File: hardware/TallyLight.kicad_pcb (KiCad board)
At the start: 4 copper layers, 68 x 68 mm, 167 parts, among them J1 Hanrun HY931147C, J2 USB_C_Receptacle_USB2.0, J3 Strapping, SW1 SW_Push, T2 HR051067, U10 EL357N(B)(TA)-G, U11 CJ431, U2 KSZ8851SNL, U3 SRV05-4, U4 ESP32-C3-WROOM-02, U5 AMS1117-3.3, U7 SRV05-4, U9 Si3402-B, Y1 25MHz

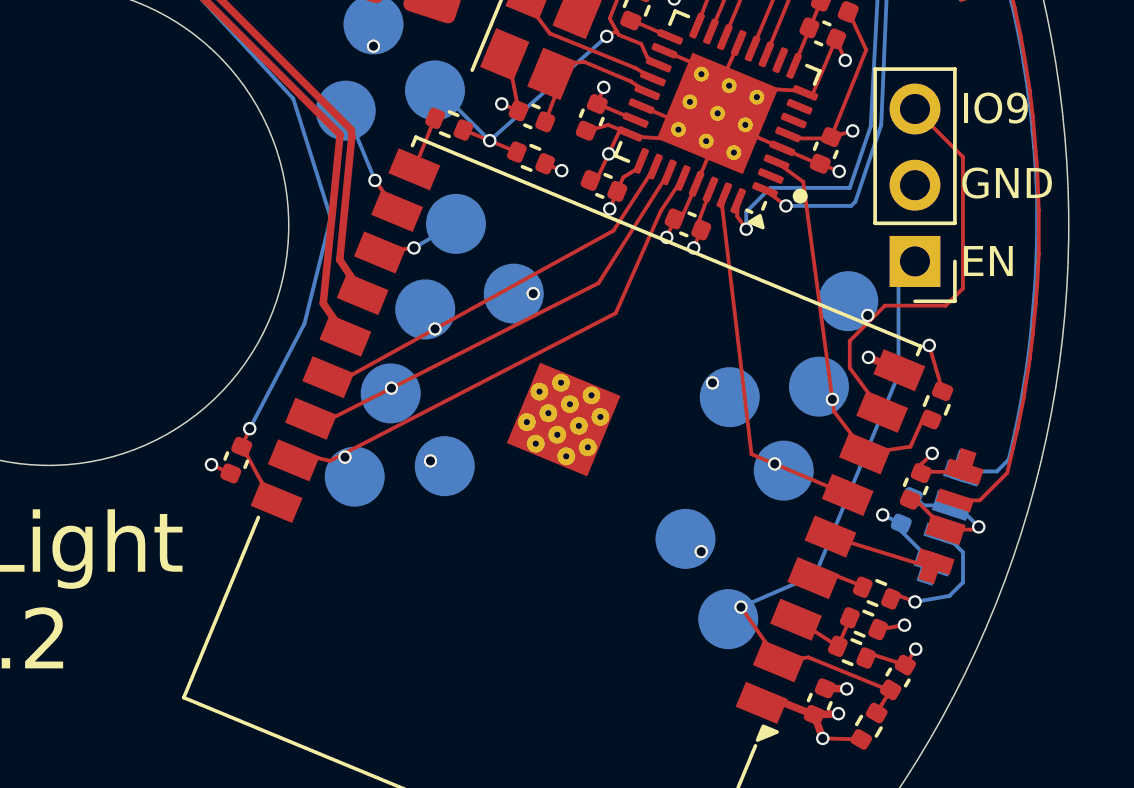
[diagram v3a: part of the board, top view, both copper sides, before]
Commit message: hardware: pull up GPIO2
There is a bit of an ominous sentence in the ESP32-C3 datasheet:
"GPIO2 actually does not determine SPI Boot and Joint Download Boot mode,
but it is recommended to pull this pin up due to glitches."

Switch GPIO2 to an input pin on the KSZ8851 and pull it up to VDD to avoid
any possible issues.
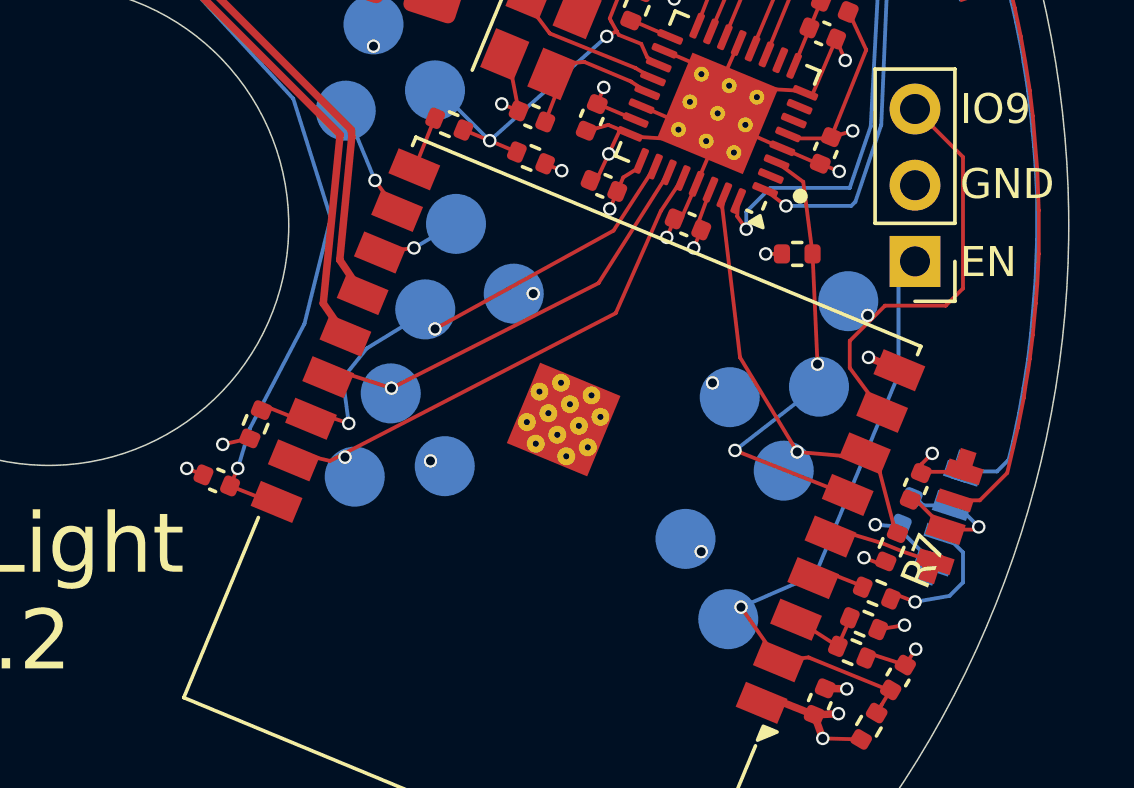
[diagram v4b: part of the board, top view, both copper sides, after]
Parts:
- added R6: 10k, Resistor_SMD:R_0402_1005Metric, F.Cu at (156.9, 106.6)
- added R7: 10k, Resistor_SMD:R_0402_1005Metric, F.Cu at (178.1, 110.7)
- moved R4 6.86 mm to (174.9, 101.0), turned to 180 degrees
- moved C14 0.94 mm to (155.6, 108.5), turned to 157.5 degrees
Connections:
- U4 pad 15: Net-(U2-~{CS}) -> Net-(U2-SO)
- U4 pad 16: Net-(U2-SO) -> Net-(U2-~{CS})
- U4 pad 6: Net-(U2-SI) -> Net-(U2-~{INT})
- U4 pad 7: Net-(U2-~{INT}) -> Net-(U2-SI)
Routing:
- net Net-(U2-~{CS}): track 13.2 -> 16.9 mm, vias 1 -> 2
- net Net-(U2-SI): track 12.2 -> 14.2 mm
- net Net-(U2-~{INT}): track 13.2 -> 14.2 mm, vias 1 -> 2
- net +3V3: track 16.2 -> 16.8 mm, vias 18 -> 20

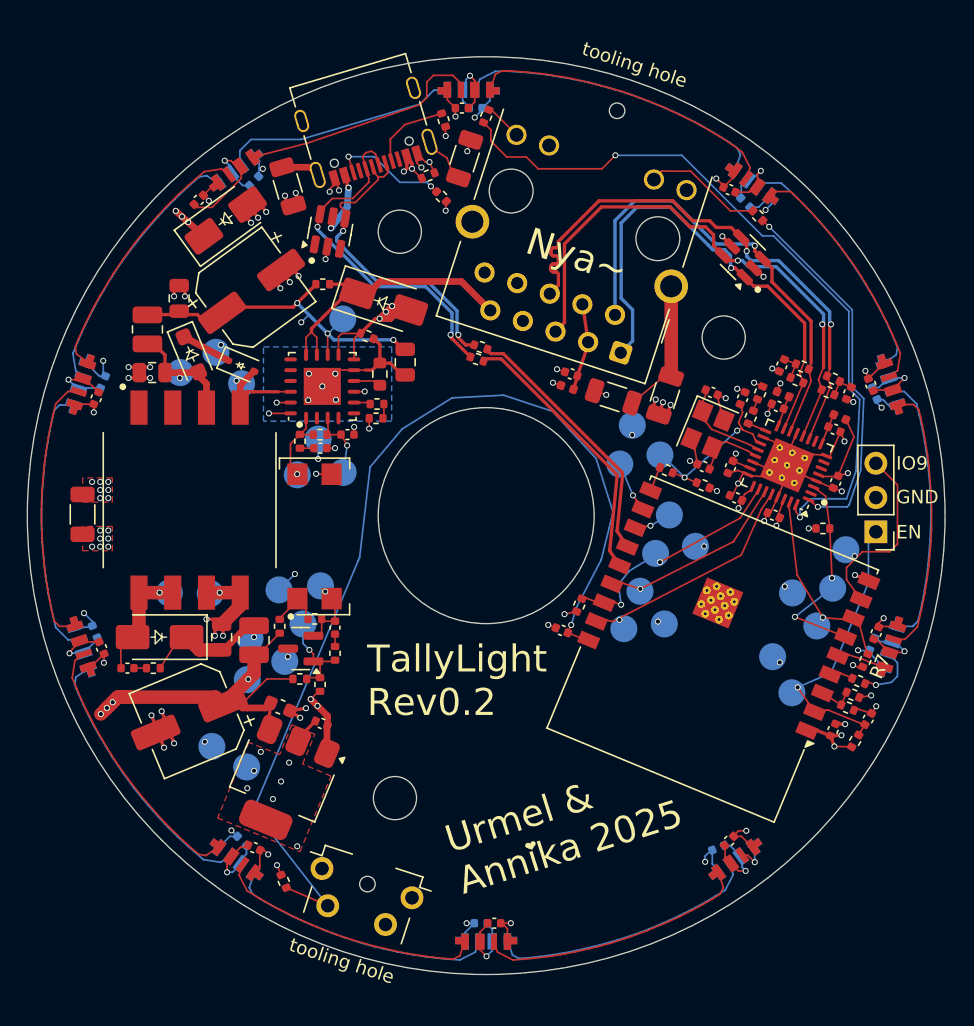
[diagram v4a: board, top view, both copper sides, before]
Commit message: hardware: add alternate snubber and flyback footprints
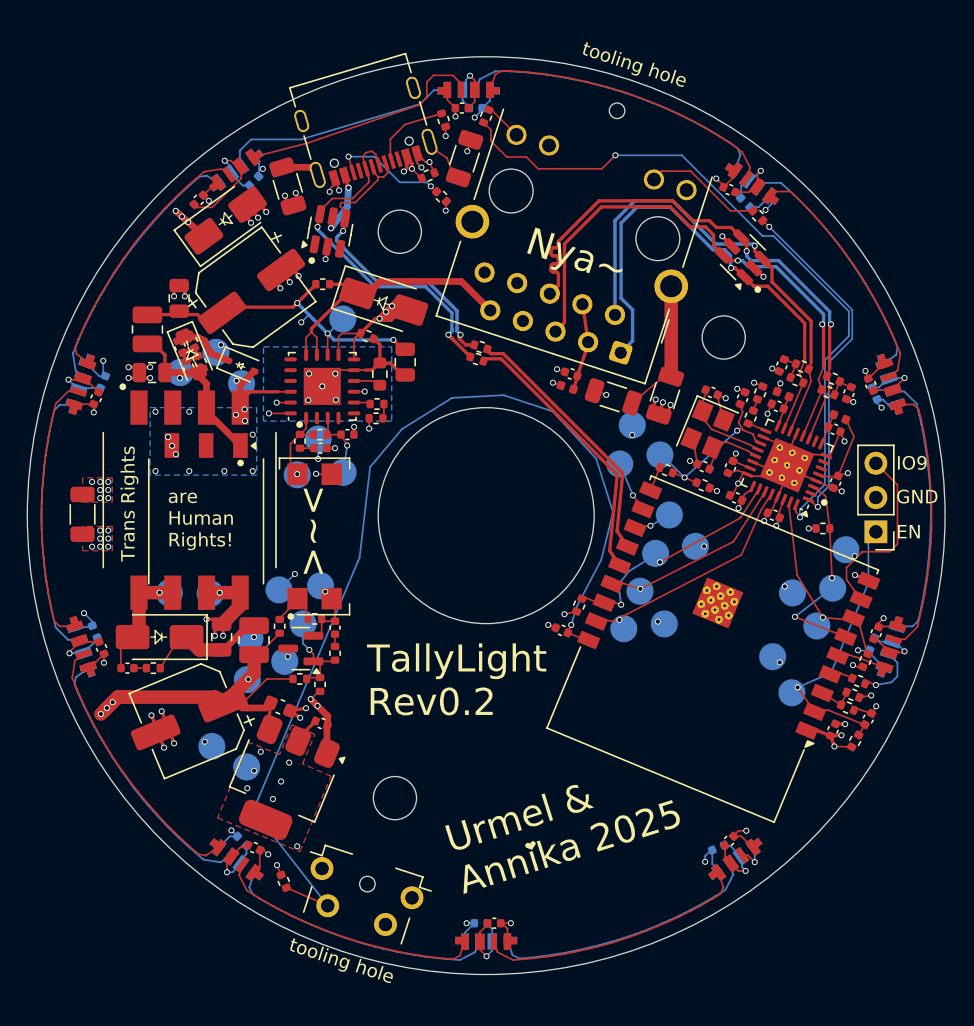
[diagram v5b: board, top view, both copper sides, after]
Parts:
- added C18: 10nF, Capacitor_SMD:C_0402_1005Metric, F.Cu at (128.0, 89.0)
- added C19: 10nF, Capacitor_SMD:C_0402_1005Metric, F.Cu at (127.3, 87.5)
- added R14: 51k, Resistor_SMD:R_0402_1005Metric, F.Cu at (128.8, 88.7)
- added R15: 51k, Resistor_SMD:R_0402_1005Metric, F.Cu at (128.2, 87.1)
- added TR1: Wuerth_750315371, Transformer_SMD:Transformer_Wuerth_750315371, F.Cu at (129.2, 100.4)
- turned TP14 to 0 degrees
- turned TP2 to 0 degrees
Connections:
- U10 pad 4: Net-(U9-EROUT) -> unconnected-(U10-Pad4)
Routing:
- net Net-(D27-A): track 7.81 -> 28.4 mm, vias 1 -> 7
- net Net-(C18-Pad2): track 0.00 -> 3.23 mm
- net Net-(D26-A2): track 8.04 -> 10.8 mm
- net /Logic/LED1: track 53.9 -> 52.2 mm
- net /Logic/LED0: track 27.6 -> 25.9 mm
- net /Logic/PoE-: track 22.6 -> 23.9 mm
- net GND2: vias 23 -> 30
- added copper zone on B.Cu, net GND2
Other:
- board text added: ">~<"
- board text added: "Trans Rights"
- board text added: "are Human Rights!"

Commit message: hardware: add LCSC partnumber to ESP32-C3 module
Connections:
- U10 pad 4: unconnected-(U10-Pad4) -> Net-(U9-EROUT)
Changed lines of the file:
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@@
 	(net 100 "unconnected-(TR1-Pad2)")
 	(net 101 "unconnected-(TR1-Pad5)")
-	(net 102 "unconnected-(U10-Pad4)")
 	(footprint "Capacitor_SMD:C_0402_1005Metric"
 		(layer "F.Cu")
@@
 			(size 1.5 1.6)
 			(layers "F.Cu" "F.Paste" "F.Mask")
-			(net 102 "unconnected-(U10-Pad4)")
+			(net 44 "Net-(U9-EROUT)")
 			(pintype "passive")
 			(thermal_bridge_angle 45)
@@
 					(thickness 0.15)
 				)
+			)
+		)
+		(property "LCSC" "C2934560"
+			(at 0 0 157.5)
+			(unlocked yes)
+			(layer "F.Fab")
+			(hide yes)
+			(effects
+				(font
+					(size 1 1)
+					(thickness 0.15)
+				)

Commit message: hardware: upgrade decoupling caps on ferrite beads to 1µF
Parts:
- C7, C8: value 100nF -> 1uF
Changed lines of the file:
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@@
 		)
 		(property "Value" "CJ431"
-			(at 0 2.4 360)
+			(at 0 2.4 0)
 			(layer "F.Fab")
 			(effects
@@
 		)
 		(property "Footprint" "Package_TO_SOT_SMD:SOT-23"
-			(at 0 0 360)
+			(at 0 0 0)
 			(layer "F.Fab")
 			(hide yes)
@@
 		)
 		(property "Datasheet" "http://www.cj-elec.com/txUpfile/20134181474991806.pdf"
-			(at 0 0 360)
+			(at 0 0 0)
 			(layer "F.Fab")
 			(hide yes)
@@
 		)
 		(property "Description" "Shunt Regulator, SOT-23"
-			(at 0 0 360)
+			(at 0 0 0)
 			(layer "F.Fab")
 			(hide yes)
@@
 		)
 		(fp_text user "${REFERENCE}"
-			(at 0 0 360)
+			(at 0 0 0)
 			(layer "F.Fab")
 			(effects
@@
 		(at 137.28 101.539999 180)
 		(property "Reference" "U10"
-			(at -3.4 0 270)
+			(at -3.4 0 -90)
 			(unlocked yes)
 			(layer "F.SilkS")
@@
 		)
 		(property "Value" "10k"
-			(at 0 1.17 360)
+			(at 0 1.17 0)
 			(layer "F.Fab")
 			(effects
@@
 		)
 		(fp_text user "${REFERENCE}"
-			(at 0 0 360)
+			(at 0 0 0)
 			(layer "F.Fab")
 			(effects
@@
 		(fp_line
 			(start -0.525 0.270001)
-			(end -0.525001 -0.269999)
+			(end -0.525001 -0.27)
 			(stroke
 				(width 0.1)
@@
 		)
 		(fp_line
-			(start -0.525001 -0.269999)
+			(start -0.525001 -0.27)
 			(end 0.525 -0.270001)
 			(stroke
@@
 		)
 		(fp_line
-			(start 0.525001 0.269999)
+			(start 0.525001 0.27)
 			(end -0.525 0.270001)
 			(stroke
@@
 		(fp_line
 			(start 0.525 -0.270001)
-			(end 0.525001 0.269999)
+			(end 0.525001 0.27)
 			(stroke
 				(width 0.1)
@@
 		)
 		(property "Value" "SS210"
-			(at 0 2.6 360)
+			(at 0 2.6 0)
 			(layer "F.Fab")
 			(effects
@@
 		)
 		(fp_text user "${REFERENCE}"
-			(at 0 -2.5 360)
+			(at 0 -2.5 0)
 			(layer "F.Fab")
 			(effects
@@
 		)
 		(property "Value" "220pF"
-			(at 0 1.16 360)
+			(at 0 1.16 0)
 			(layer "F.Fab")
 			(effects
@@
 		)
 		(fp_text user "${REFERENCE}"
-			(at 0 0 360)
+			(at 0 0 0)
 			(layer "F.Fab")
 			(effects
@@
 			)
 		)
-		(property "Value" "100nF"
+		(property "Value" "1uF"
 			(at 0 1.16 157.5)
 			(layer "F.Fab")
@@
 			)
 		)
-		(property "LCSC" "C1525"
+		(property "LCSC" "C52923"
 			(at 0 0 -22.5)
 			(unlocked yes)
@@
 		(fp_line
 			(start -0.64944 0.001019)
-			(end -1.55114 0.001021)
+			(end -1.551139 0.001021)
 			(stroke
 				(width 0.1)
@@
 		)
 		(property "Value" "10uF"
-			(at 0 1.16 162)
+			(at 0 1.160001 162)
 			(layer "F.Fab")
 			(effects
@@
 		)
 		(fp_line
-			(start -3.410001 -2.345562)
+			(start -3.410002 -2.345562)
 			(end -2.345563 -3.41)
 			(stroke
@@
 		)
 		(fp_line
-			(start -3.410001 -2.345562)
+			(start -3.410002 -2.345562)
 			(end -3.410001 -1.059999)
 			(stroke
@@
 		(fp_line
 			(start -3.41 2.345563)
-			(end -2.345562 3.410001)
+			(end -2.345562 3.410002)
 			(stroke
 				(width 0.12)
@@
 		)
 		(fp_line
-			(start -2.345562 3.410001)
+			(start -2.345562 3.410002)
 			(end 3.409999 3.41)
 			(stroke
@@
 		)
 		(property "Value" "100nF HV"
-			(at -0.000001 1.68 360)
+			(at -0.000001 1.68 0)
 			(layer "F.Fab")
 			(effects
@@
 		)
 		(fp_text user "${REFERENCE}"
-			(at 0 0 360)
+			(at 0 0 0)
 			(layer "F.Fab")
 			(effects
@@
 		)
 		(property "Value" "0"
-			(at 0 1.17 360)
+			(at 0 1.17 0)
 			(layer "F.Fab")
 			(effects
@@
 		)
 		(fp_text user "${REFERENCE}"
-			(at 0 0 360)
+			(at 0 0 0)
 			(layer "F.Fab")
 			(effects
@@
 			)
 		)
-		(property "Value" "100nF"
+		(property "Value" "1uF"
 			(at 0 1.16 157.5)
 			(layer "F.Fab")
@@
 			)
 		)
-		(property "LCSC" "C1525"
+		(property "LCSC" "C52923"
 			(at 0 0 157.5)
 			(unlocked yes)
@@
 		)
 		(property "Value" "4.7k"
-			(at 0 1.17 360)
+			(at 0 1.17 0)
 			(layer "F.Fab")
 			(effects
@@
 		)
 		(fp_text user "${REFERENCE}"
-			(at 0 0 360)
+			(at 0 0 0)
 			(layer "F.Fab")
 			(effects
@@
 		(fp_line
 			(start -8.500001 -6.000001)
-			(end -8.999998 -5.500001)
+			(end -8.999998 -5.5)
 			(stroke
 				(width 0.1)
@@
 		)
 		(fp_line
-			(start -8.999998 -5.500001)
+			(start -8.999998 -5.5)
 			(end -9 6.9)
 			(stroke
@@
 		)
 		(pad "19" thru_hole circle
-			(at 2.06 0.75 157.5)
+			(at 2.06 0.750001 157.5)
 			(size 0.6 0.6)
 			(drill 0.2)
@@
 		)
 		(property "Value" "Strapping"
-			(at 0 7.41 360)
+			(at 0 7.41 0)
 			(layer "F.Fab")
 			(effects
@@
 		(fp_line
 			(start -0.649439 0.001019)
-			(end 0.501179 0.750318)
+			(end 0.50118 0.750318)
 			(stroke
 				(width 0.1)
@@
 		)
 		(fp_line
-			(start 0.501179 0.750318)
+			(start 0.50118 0.750318)
 			(end 0.501181 -0.799081)
 			(stroke
@@
 		)
 		(property "Value" "HR051067"
-			(at 0 0 360)
+			(at 0 0 0)
 			(layer "F.Fab")
 			(effects
@@
 		)
 		(property "Footprint" "Transformer_HanRun:HR051067"
-			(at 0 0 360)
+			(at 0 0 0)
 			(layer "F.Fab")
 			(hide yes)
@@
 		)
 		(property "Datasheet" "https://www.lcsc.com/datasheet/lcsc_datasheet_2409302201_HANRUN-Zhongshan-HanRun-Elec-HR051067_C93830.pdf"
-			(at 0 0 360)
+			(at 0 0 0)
 			(layer "F.Fab")
 			(hide yes)
@@
 		)
 		(property "Description" ""
-			(at 0 0 360)
+			(at 0 0 0)
 			(layer "F.Fab")
 			(hide yes)
@@
 		(tags "test point SMD pad")
 		(property "Reference" "TP14"
-			(at 0 3.000001 360)
+			(at 0 3.000001 0)
 			(layer "B.SilkS")
 			(hide yes)
@@
 		)
 		(property "Value" "GND2"
-			(at 0 -2.05 360)
+			(at 0 -2.05 0)
 			(layer "B.Fab")
 			(effects
@@
 		)
 		(fp_text user "${REFERENCE}"
-			(at 0.000001 2 360)
+			(at 0.000001 2 0)
 			(layer "B.Fab")
 			(effects

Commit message: Implement review comments by Urmel
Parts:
- added C20: 100nF, Capacitor_SMD:C_0402_1005Metric, F.Cu at (149.3, 87.7)
- added C21: 100nF, Capacitor_SMD:C_0402_1005Metric, F.Cu at (148.5, 89.5)
- added C22: 100nF, Capacitor_SMD:C_0402_1005Metric, F.Cu at (176.2, 85.9)
- added C23: 100nF, Capacitor_SMD:C_0402_1005Metric, F.Cu at (174.3, 85.9)
- added R16: 100R, Resistor_SMD:R_0402_1005Metric, F.Cu at (135.5, 125.4)
- C57: value 15nF -> 1nF
- moved R44 2.29 mm to (151.2, 89.1), turned to 157.5 degrees
- moved R45 2.21 mm to (150.9, 90.0), turned to -22.5 degrees
- moved R28 0.78 mm to (135.1, 126.3), turned to -22.5 degrees
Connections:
- R28 pad 2: /Logic/BUTTON -> Net-(R16-Pad1)
- SW1 pad 1: /Logic/BUTTON -> Net-(R16-Pad1)
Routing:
- net /Logic/BUTTON: track 74.8 -> 66.5 mm, vias 1 -> 2
- net Net-(R16-Pad1): track 0.00 -> 4.60 mm
- net GND: track 145.4 -> 148.7 mm, vias 78 -> 83
- net /Logic/D-: track 19.7 -> 16.5 mm
- net /Logic/D+: track 20.4 -> 17.6 mm
- net /Logic/IO9: track 14.0 -> 11.5 mm
- net +3V3: track 16.8 -> 18.9 mm, vias 20 -> 24
- net /Logic/USB/conn_D-: track 23.9 -> 25.8 mm
- net /Logic/USB/conn_D+: track 26.6 -> 28.2 mm
- net /Logic/LED0: track 25.9 -> 26.9 mm
- net /Logic/MDI_RX+: track 40.9 -> 39.9 mm
- net /Logic/LED1: track 52.2 -> 52.8 mm
- net /Logic/MDI_RX-: track 40.3 -> 40.8 mm
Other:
- board text added: "TallyLight Rev0.3"
- board text removed: "+"
- board text removed: "TallyLight Rev0.2"
